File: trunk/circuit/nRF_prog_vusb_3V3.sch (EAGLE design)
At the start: 33 parts, among them Q1 12MHz

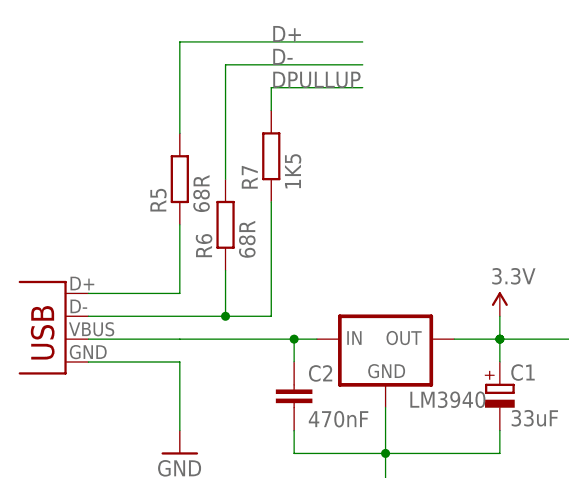
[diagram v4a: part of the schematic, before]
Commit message: added testpins for USB
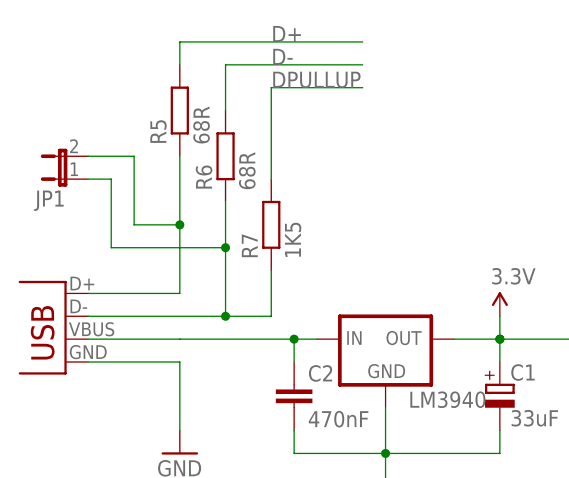
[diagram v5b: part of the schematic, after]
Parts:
- added JP1: (no value), KileParts:JP1E
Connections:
- net USB_D+: now also JP1.2
- net USB_D-: now also JP1.1
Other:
- moved on the sheet: R5, R6, R7
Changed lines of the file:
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@@
 <grid distance="0.1" unitdist="inch" unit="inch" style="lines" multiple="1" display="no" altdistance="0.01" altunitdist="inch" altunit="inch"/>
 <layers>
-<layer number="1" name="Top" color="4" fill="1" visible="yes" active="no"/>
-<layer number="16" name="Bottom" color="1" fill="1" visible="yes" active="no"/>
-<layer number="17" name="Pads" color="2" fill="1" visible="yes" active="no"/>
-<layer number="18" name="Vias" color="2" fill="1" visible="yes" active="no"/>
-<layer number="19" name="Unrouted" color="6" fill="1" visible="yes" active="no"/>
-<layer number="20" name="Dimension" color="15" fill="1" visible="yes" active="no"/>
-<layer number="21" name="tPlace" color="7" fill="1" visible="yes" active="no"/>
-<layer number="22" name="bPlace" color="7" fill="1" visible="yes" active="no"/>
-<layer number="23" name="tOrigins" color="15" fill="1" visible="yes" active="no"/>
-<layer number="24" name="bOrigins" color="15" fill="1" visible="yes" active="no"/>
-<layer number="25" name="tNames" color="7" fill="1" visible="yes" active="no"/>
-<layer number="26" name="bNames" color="7" fill="1" visible="yes" active="no"/>
-<layer number="27" name="tValues" color="7" fill="1" visible="yes" active="no"/>
-<layer number="28" name="bValues" color="7" fill="1" visible="yes" active="no"/>
+<layer number="1" name="Top" color="4" fill="1" visible="no" active="no"/>
+<layer number="16" name="Bottom" color="1" fill="1" visible="no" active="no"/>
+<layer number="17" name="Pads" color="2" fill="1" visible="no" active="no"/>
+<layer number="18" name="Vias" color="2" fill="1" visible="no" active="no"/>
+<layer number="19" name="Unrouted" color="6" fill="1" visible="no" active="no"/>
+<layer number="20" name="Dimension" color="15" fill="1" visible="no" active="no"/>
+<layer number="21" name="tPlace" color="7" fill="1" visible="no" active="no"/>
+<layer number="22" name="bPlace" color="7" fill="1" visible="no" active="no"/>
+<layer number="23" name="tOrigins" color="15" fill="1" visible="no" active="no"/>
+<layer number="24" name="bOrigins" color="15" fill="1" visible="no" active="no"/>
+<layer number="25" name="tNames" color="7" fill="1" visible="no" active="no"/>
+<layer number="26" name="bNames" color="7" fill="1" visible="no" active="no"/>
+<layer number="27" name="tValues" color="7" fill="1" visible="no" active="no"/>
+<layer number="28" name="bValues" color="7" fill="1" visible="no" active="no"/>
 <layer number="29" name="tStop" color="7" fill="3" visible="no" active="no"/>
 <layer number="30" name="bStop" color="7" fill="6" visible="no" active="no"/>
@@
 <layer number="35" name="tGlue" color="7" fill="4" visible="no" active="no"/>
 <layer number="36" name="bGlue" color="7" fill="5" visible="no" active="no"/>
-<layer number="37" name="tTest" color="7" fill="1" visible="yes" active="no"/>
-<layer number="38" name="bTest" color="7" fill="1" visible="yes" active="no"/>
+<layer number="37" name="tTest" color="7" fill="1" visible="no" active="no"/>
+<layer number="38" name="bTest" color="7" fill="1" visible="no" active="no"/>
 <layer number="39" name="tKeepout" color="4" fill="11" visible="no" active="no"/>
 <layer number="40" name="bKeepout" color="1" fill="11" visible="no" active="no"/>
@@
 <layer number="44" name="Drills" color="7" fill="1" visible="no" active="no"/>
 <layer number="45" name="Holes" color="7" fill="1" visible="no" active="no"/>
-<layer number="46" name="Milling" color="3" fill="1" visible="yes" active="no"/>
-<layer number="47" name="Measures" color="7" fill="1" visible="yes" active="no"/>
-<layer number="48" name="Document" color="7" fill="1" visible="yes" active="no"/>
-<layer number="49" name="Reference" color="7" fill="1" visible="yes" active="no"/>
-<layer number="50" name="dxf" color="7" fill="1" visible="yes" active="no"/>
-<layer number="51" name="tDocu" color="7" fill="1" visible="yes" active="no"/>
-<layer number="52" name="bDocu" color="7" fill="1" visible="yes" active="no"/>
-<layer number="53" name="tGND_GNDA" color="7" fill="9" visible="yes" active="no"/>
-<layer number="54" name="bGND_GNDA" color="1" fill="9" visible="yes" active="no"/>
-<layer number="56" name="wert" color="7" fill="1" visible="yes" active="no"/>
-<layer number="57" name="tCAD" color="7" fill="1" visible="yes" active="no"/>
+<layer number="46" name="Milling" color="3" fill="1" visible="no" active="no"/>
+<layer number="47" name="Measures" color="7" fill="1" visible="no" active="no"/>
+<layer number="48" name="Document" color="7" fill="1" visible="no" active="no"/>
+<layer number="49" name="Reference" color="7" fill="1" visible="no" active="no"/>
+<layer number="50" name="dxf" color="7" fill="1" visible="no" active="no"/>
+<layer number="51" name="tDocu" color="7" fill="1" visible="no" active="no"/>
+<layer number="52" name="bDocu" color="7" fill="1" visible="no" active="no"/>
+<layer number="53" name="tGND_GNDA" color="7" fill="9" visible="no" active="no"/>
+<layer number="54" name="bGND_GNDA" color="1" fill="9" visible="no" active="no"/>
+<layer number="56" name="wert" color="7" fill="1" visible="no" active="no"/>
+<layer number="57" name="tCAD" color="7" fill="1" visible="no" active="no"/>
 <layer number="91" name="Nets" color="2" fill="1" visible="yes" active="yes"/>
 <layer number="92" name="Busses" color="1" fill="1" visible="yes" active="yes"/>
@@
 <part name="C4" library="rcl" deviceset="CPOL-EU" device="SMCB" value="10uF"/>
 <part name="U$2" library="SparkFun" deviceset="OSHW-LOGO" device="L" value="OSHW-LOGOL"/>
+<part name="JP1" library="KileParts" deviceset="JP1E" device=""/>
 </parts>
 <sheets>
@@
 <instance part="USB-B" gate="G$1" x="-38.1" y="88.9" rot="MR0"/>
 <instance part="GND6" gate="1" x="-25.4" y="78.74"/>
-<instance part="R5" gate="G$1" x="-25.4" y="109.22" rot="R90"/>
-<instance part="R6" gate="G$1" x="-20.32" y="104.14" rot="R90"/>
-<instance part="R7" gate="G$1" x="-15.24" y="111.76" rot="R90"/>
+<instance part="R5" gate="G$1" x="-25.4" y="116.84" rot="R90"/>
+<instance part="R6" gate="G$1" x="-20.32" y="111.76" rot="R90"/>
+<instance part="R7" gate="G$1" x="-15.24" y="104.14" rot="R90"/>
 <instance part="C5" gate="G$1" x="127" y="43.18"/>
 <instance part="AVR_RST" gate="G$1" x="50.8" y="101.6" rot="MR0"/>
@@
 <instance part="C4" gate="G$1" x="175.26" y="10.16"/>
 <instance part="U$2" gate="G$1" x="-12.7" y="27.94"/>
+<instance part="JP1" gate="A" x="-38.1" y="109.22" rot="R90"/>
 </instances>
 <busses>
@@
 <pinref part="R5" gate="G$1" pin="1"/>
 <wire x1="-25.4" y1="96.52" x2="-25.4" y2="104.14" width="0.1524" layer="91"/>
+<pinref part="JP1" gate="A" pin="2"/>
+<wire x1="-25.4" y1="104.14" x2="-25.4" y2="111.76" width="0.1524" layer="91"/>
+<wire x1="-35.56" y1="111.76" x2="-30.48" y2="111.76" width="0.1524" layer="91"/>
+<wire x1="-30.48" y1="111.76" x2="-30.48" y2="104.14" width="0.1524" layer="91"/>
+<wire x1="-30.48" y1="104.14" x2="-25.4" y2="104.14" width="0.1524" layer="91"/>
+<junction x="-25.4" y="104.14"/>
 </segment>
 </net>
@@
 <wire x1="-35.56" y1="93.98" x2="-20.32" y2="93.98" width="0.1524" layer="91"/>
 <pinref part="R6" gate="G$1" pin="1"/>
-<wire x1="-20.32" y1="93.98" x2="-20.32" y2="99.06" width="0.1524" layer="91"/>
+<wire x1="-20.32" y1="93.98" x2="-20.32" y2="101.6" width="0.1524" layer="91"/>
 <junction x="-20.32" y="93.98"/>
 <pinref part="R7" gate="G$1" pin="1"/>
-<wire x1="-15.24" y1="106.68" x2="-15.24" y2="93.98" width="0.1524" layer="91"/>
+<wire x1="-20.32" y1="101.6" x2="-20.32" y2="106.68" width="0.1524" layer="91"/>
+<wire x1="-15.24" y1="99.06" x2="-15.24" y2="93.98" width="0.1524" layer="91"/>
 <wire x1="-15.24" y1="93.98" x2="-20.32" y2="93.98" width="0.1524" layer="91"/>
+<pinref part="JP1" gate="A" pin="1"/>
+<wire x1="-35.56" y1="109.22" x2="-33.02" y2="109.22" width="0.1524" layer="91"/>
+<wire x1="-33.02" y1="109.22" x2="-33.02" y2="101.6" width="0.1524" layer="91"/>
+<wire x1="-33.02" y1="101.6" x2="-20.32" y2="101.6" width="0.1524" layer="91"/>
+<junction x="-20.32" y="101.6"/>
 </segment>
 </net>
@@
 <segment>
 <pinref part="R5" gate="G$1" pin="2"/>
-<wire x1="-25.4" y1="114.3" x2="-25.4" y2="124.46" width="0.1524" layer="91"/>
+<wire x1="-25.4" y1="121.92" x2="-25.4" y2="124.46" width="0.1524" layer="91"/>
 <wire x1="-25.4" y1="124.46" x2="-5.08" y2="124.46" width="0.1524" layer="91"/>
 <label x="-15.24" y="124.46" size="1.778" layer="95"/>
@@
 <segment>
 <pinref part="R6" gate="G$1" pin="2"/>
-<wire x1="-20.32" y1="109.22" x2="-20.32" y2="121.92" width="0.1524" layer="91"/>
+<wire x1="-20.32" y1="116.84" x2="-20.32" y2="121.92" width="0.1524" layer="91"/>
 <wire x1="-20.32" y1="121.92" x2="-5.08" y2="121.92" width="0.1524" layer="91"/>
 <label x="-15.24" y="121.92" size="1.778" layer="95"/>
@@
 <segment>
 <pinref part="R7" gate="G$1" pin="2"/>
-<wire x1="-15.24" y1="116.84" x2="-15.24" y2="119.38" width="0.1524" layer="91"/>
+<wire x1="-15.24" y1="109.22" x2="-15.24" y2="119.38" width="0.1524" layer="91"/>
 <wire x1="-15.24" y1="119.38" x2="-5.08" y2="119.38" width="0.1524" layer="91"/>
 <label x="-15.24" y="119.38" size="1.778" layer="95"/>

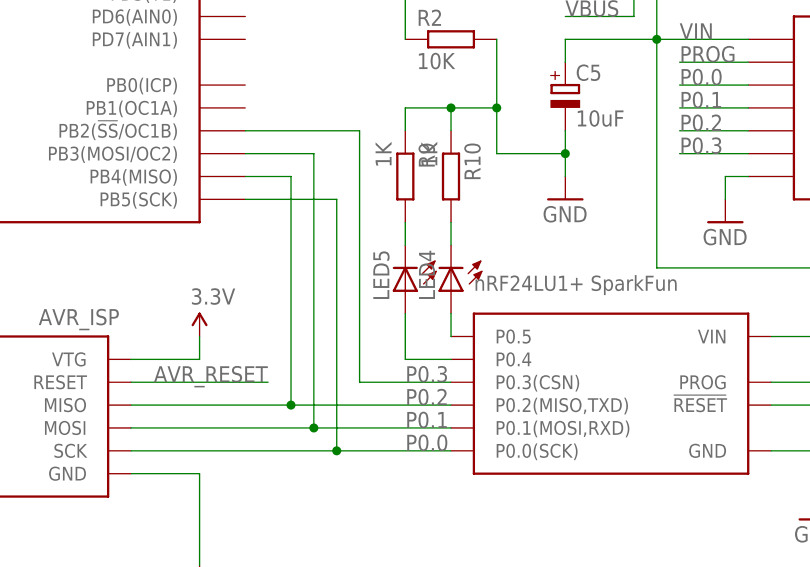
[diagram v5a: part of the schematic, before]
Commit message: 
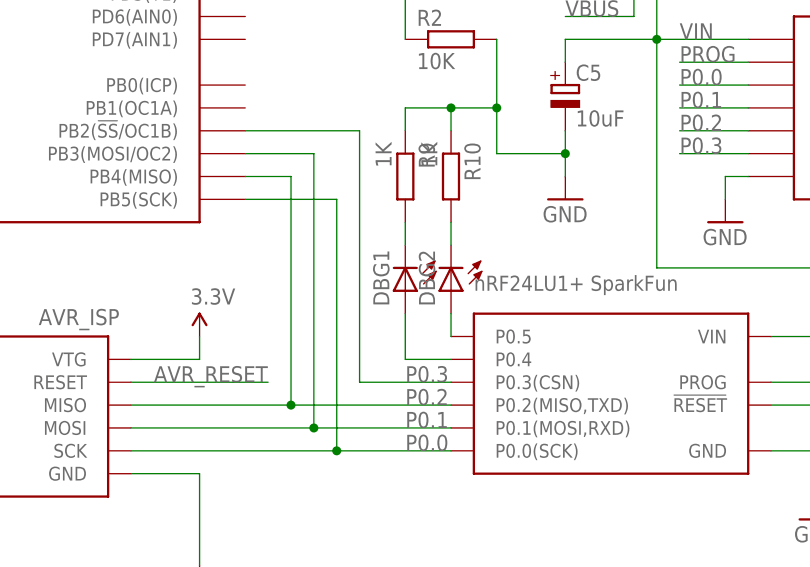
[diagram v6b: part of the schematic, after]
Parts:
- renumbered LED4 to DBG2, LED5 to DBG1
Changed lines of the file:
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@@
 <part name="TGT_PWR" library="KileParts" deviceset="JP2E" device=""/>
 <part name="P+4" library="SparkFun" deviceset="3.3V" device=""/>
-<part name="LED4" library="led" deviceset="LED" device="CHIPLED_0805"/>
-<part name="LED5" library="led" deviceset="LED" device="CHIPLED_0805"/>
+<part name="DBG2" library="led" deviceset="LED" device="CHIPLED_0805"/>
+<part name="DBG1" library="led" deviceset="LED" device="CHIPLED_0805"/>
 <part name="R9" library="rcl" deviceset="R-EU_" device="M0805" value="1K"/>
 <part name="R10" library="rcl" deviceset="R-EU_" device="M0805" value="1K"/>
@@
 <instance part="TGT_PWR" gate="1" x="137.16" y="63.5"/>
 <instance part="P+4" gate="G$1" x="147.32" y="60.96"/>
-<instance part="LED4" gate="G$1" x="114.3" y="20.32" rot="R180"/>
-<instance part="LED5" gate="G$1" x="109.22" y="20.32" rot="R180"/>
+<instance part="DBG2" gate="G$1" x="114.3" y="20.32" rot="R180"/>
+<instance part="DBG1" gate="G$1" x="109.22" y="20.32" rot="R180"/>
 <instance part="R9" gate="G$1" x="109.22" y="33.02" rot="R270"/>
 <instance part="R10" gate="G$1" x="114.3" y="33.02" rot="R270"/>
@@
 <segment>
 <pinref part="LU1+_SPARKFUN" gate="G$1" pin="P0.5"/>
-<pinref part="LED4" gate="G$1" pin="A"/>
+<pinref part="DBG2" gate="G$1" pin="A"/>
 <wire x1="114.3" y1="15.24" x2="114.3" y2="17.78" width="0.1524" layer="91"/>
 </segment>
@@
 <segment>
 <pinref part="LU1+_SPARKFUN" gate="G$1" pin="P0.4"/>
-<pinref part="LED5" gate="G$1" pin="A"/>
+<pinref part="DBG1" gate="G$1" pin="A"/>
 <wire x1="114.3" y1="12.7" x2="109.22" y2="12.7" width="0.1524" layer="91"/>
 <wire x1="109.22" y1="12.7" x2="109.22" y2="17.78" width="0.1524" layer="91"/>
@@
 <net name="N$3" class="0">
 <segment>
-<pinref part="LED4" gate="G$1" pin="C"/>
+<pinref part="DBG2" gate="G$1" pin="C"/>
 <pinref part="R10" gate="G$1" pin="2"/>
 <wire x1="114.3" y1="27.94" x2="114.3" y2="25.4" width="0.1524" layer="91"/>
@@
 <net name="N$4" class="0">
 <segment>
-<pinref part="LED5" gate="G$1" pin="C"/>
+<pinref part="DBG1" gate="G$1" pin="C"/>
 <pinref part="R9" gate="G$1" pin="2"/>
 <wire x1="109.22" y1="25.4" x2="109.22" y2="27.94" width="0.1524" layer="91"/>
